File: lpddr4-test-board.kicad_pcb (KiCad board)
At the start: 8 copper layers, 117 x 81 mm, 261 parts, among them IC1 TPS54561, IC2 NCP380HMUAJAATBG, IC3 TPD8S009DSMR, J1 0878311420, J2 08B0-1X1T-36-F, J3 DC_SOCKET, J4 WE_629105150521, J5 61300611121, J6 685119134923, J7 1140084168, J8 61300411121, J9 ddr3-sodimm-slot-2-2013289-2, Q1 BC817W, Q2 BSS138AKA, Q3 BSS138AKA, Q4 BSS138AKA, Q5 BSS138AKA, Q6 BSS138AKA, U1 XC7K70T-FBG484, U10 REF3012AIDBZT, U12 FT2232HQ, U2 ASEM1-100.000MHZ-LC-T, U3 S25FL128SAGNFI000, U4 TPS65296, U5 TPS62823DLCT, U6 DP83848JSQ_NOPB, Y1 ABM8G-25.000MHZ-18-D2Y-T

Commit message: Activate B16
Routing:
- net Net-(J2-Pad8): track 0.00 -> 4.31 mm
- net GND: track 255.3 -> 257.7 mm, vias 218 -> 222
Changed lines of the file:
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@@
     (thickness 1.6)
     (drawings 130)
-    (tracks 4502)
+    (tracks 4514)
     (zones 0)
     (modules 261)
@@
   (via (at 103 128) (size 3.2) (drill 3) (layers F.Cu B.Cu) (net 0))
   (via (at 214 128) (size 3.2) (drill 3) (layers F.Cu B.Cu) (net 0))
+  (via (at 198.521 104.047) (size 0.5) (drill 0.2) (layers F.Cu B.Cu) (net 35))
+  (segment (start 198.511 103.455) (end 198.511 104.037) (width 0.15) (layer B.Cu) (net 35))
+  (via (at 200.426 104.047) (size 0.5) (drill 0.2) (layers F.Cu B.Cu) (net 35))
+  (segment (start 200.416 103.455) (end 200.416 104.037) (width 0.15) (layer B.Cu) (net 35))
+  (via (at 202.458 104.047) (size 0.5) (drill 0.2) (layers F.Cu B.Cu) (net 35))
+  (segment (start 202.448 103.455) (end 202.448 104.037) (width 0.15) (layer B.Cu) (net 35))
   (segment (start 173.536329 104.497157) (end 174.036329 104.997157) (width 0.15) (layer F.Cu) (net 392))
   (via blind (at 174.036329 104.997157) (size 0.5) (drill 0.2) (layers F.Cu GND1) (net 392) (status 40000))
@@
   (segment (start 171.536329 91.497157) (end 172.036329 90.997156) (width 0.15) (layer F.Cu) (net 19))
   (via (at 172.036329 90.997156) (size 0.5) (drill 0.2) (layers F.Cu B.Cu) (net 19) (status 40000))
+  (segment (start 207.465 101.47) (end 207.465 102.977) (width 0.15) (layer B.Cu) (net 21))
+  (segment (start 206.5736 103.8684) (end 206.5736 105.4102) (width 0.15) (layer B.Cu) (net 21))
+  (segment (start 207.465 102.977) (end 206.5736 103.8684) (width 0.15) (layer B.Cu) (net 21))
   (via (at 168.036329 90.997157) (size 0.5) (drill 0.2) (layers F.Cu B.Cu) (net 29) (status 40000))
   (segment (start 168.536329 91.497157) (end 168.036329 90.997157) (width 0.15) (layer F.Cu) (net 29))
@@
   (segment (start 207.528 70.273) (end 208.673 70.273) (width 0.15) (layer F.Cu) (net 35))
   (segment (start 208.673 70.273) (end 208.681 70.265) (width 0.15) (layer F.Cu) (net 35))
+  (via (at 204.49 104.047) (size 0.5) (drill 0.2) (layers F.Cu B.Cu) (net 35))
+  (segment (start 204.48 103.455) (end 204.48 104.037) (width 0.15) (layer B.Cu) (net 35))
+  (segment (start 204.48 104.037) (end 204.49 104.047) (width 0.15) (layer B.Cu) (net 35))
   (segment (start 163.536329 104.497157) (end 163.036329 104.997157) (width 0.15) (layer F.Cu) (net 36))
   (via (at 163.036329 104.997157) (size 0.5) (drill 0.2) (layers F.Cu B.Cu) (net 36) (status 40000))

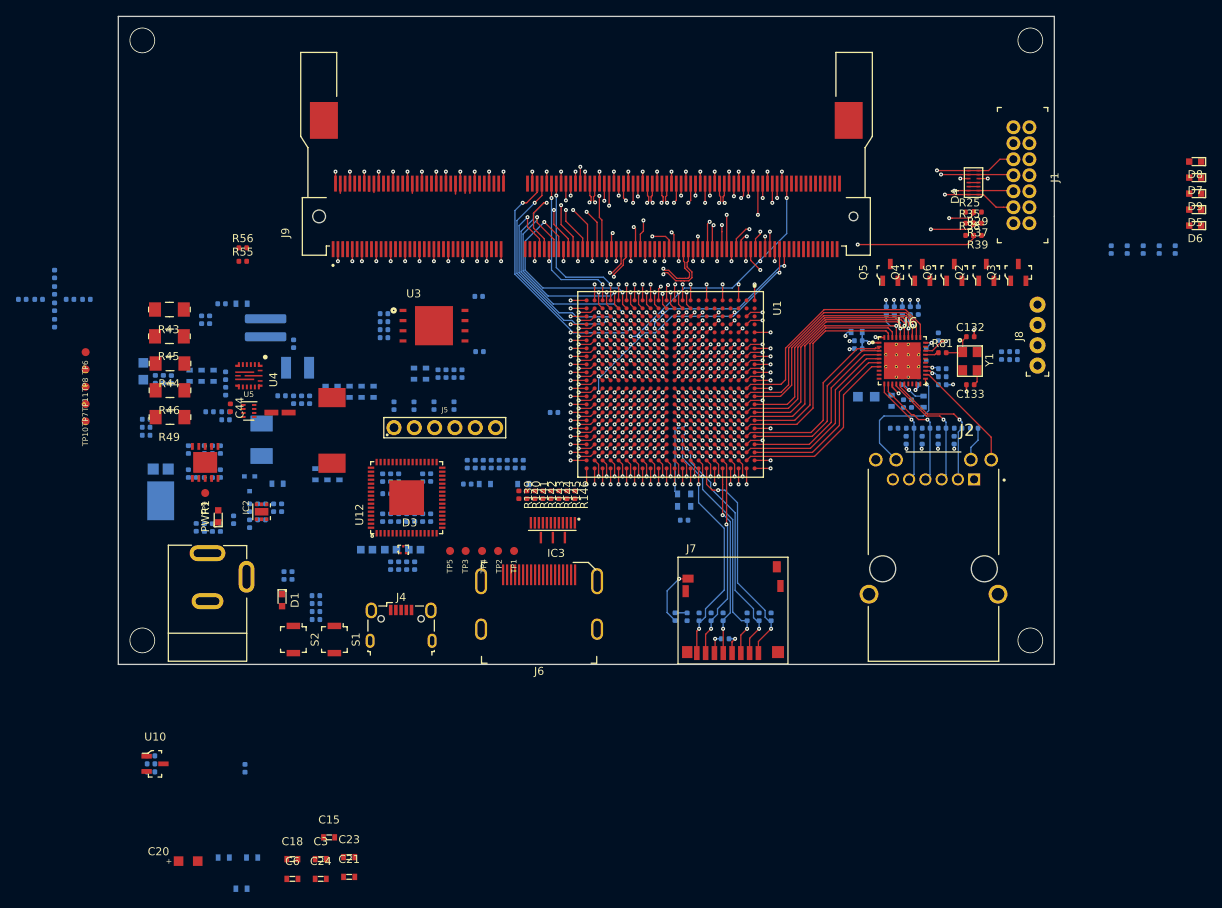
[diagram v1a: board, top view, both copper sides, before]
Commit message: Route SD card
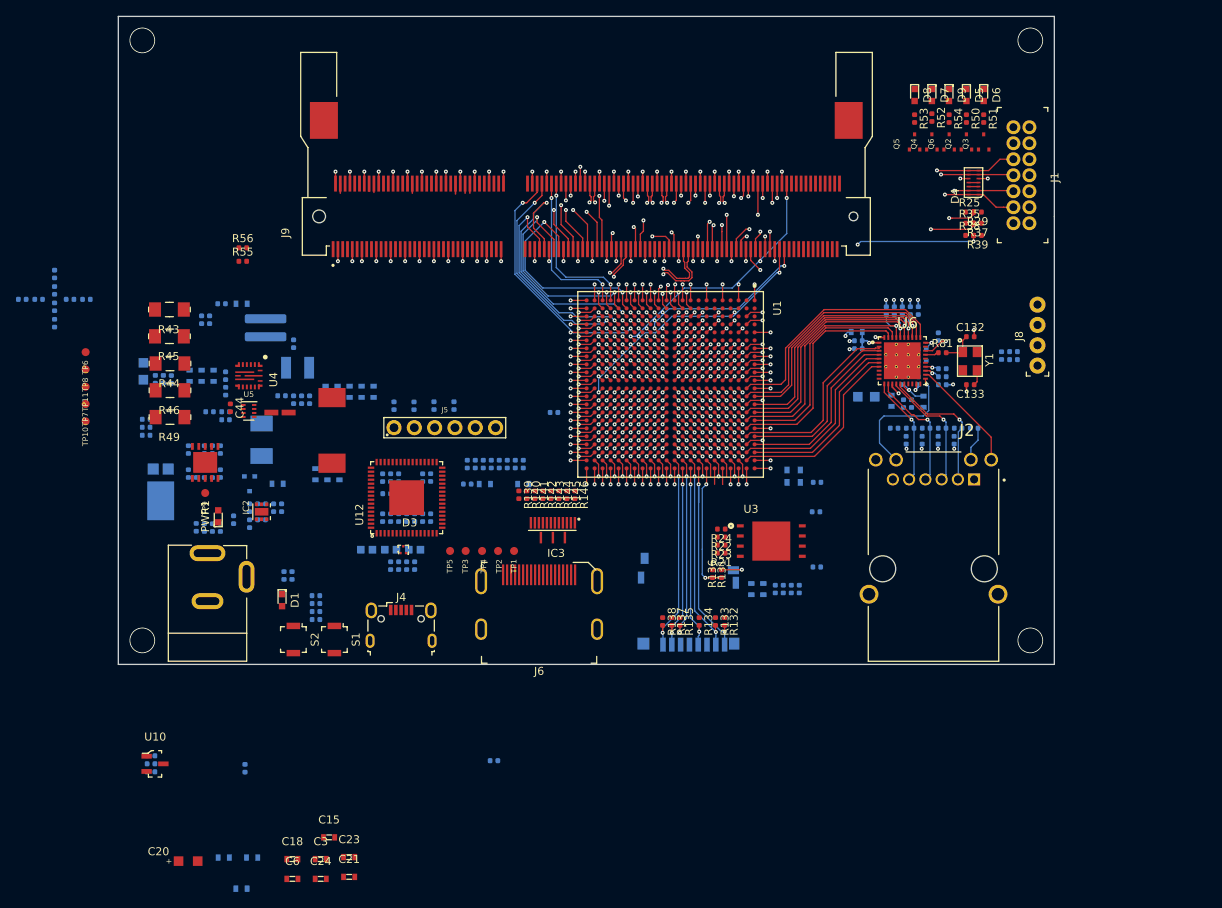
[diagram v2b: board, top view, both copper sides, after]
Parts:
- J7: moved to B.Cu
- Q2, Q3, Q4, Q5, Q6: value BSS138AKA -> BSS138APW; footprint lpddr4-test-board-footprints:SOT-23-3 -> antmicro-footprints:SC70-3
- R131, R132, R133, R134, R135, R136, R137, R138, R21, R22, R23, R24, R50, R51, R52, R53, R54: moved to F.Cu
- moved C5 50.0 mm to (187.2, 111.9)
- moved R10 50.0 mm to (183.1, 121.6)
- moved R20 50.0 mm to (182.1, 121.6)
- moved R21 50.0 mm to (175.4, 117.1)
- moved R22 50.0 mm to (175.4, 115.1)
- moved R23 50.0 mm to (175.4, 116.1)
- moved R24 50.0 mm to (175.4, 114.1)
- moved R26 50.0 mm to (179.1, 121.6)
- moved R27 50.0 mm to (180.6, 121.6)
- moved R33 50.0 mm to (185.1, 121.6)
- moved R34 50.0 mm to (184.1, 121.6)
- moved U3 50.0 mm to (181.6, 115.6)
- moved C10 50.0 mm to (187.3, 118.8)
- moved D8 36.1 mm to (199.5, 59.8), turned to 270 degrees
- moved D7 34.5 mm to (201.7, 59.8), turned to 270 degrees
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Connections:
- net DAT1 renamed SD_DAT1
- J7 pad 1: DAT2 -> SD_DAT2
- J7 pad 2: CD_DAT3 -> SD_DAT3
- J7 pad 3: MOSI_CMD -> SD_CMD
- J7 pad 5: SCK -> SD_CLK
- J7 pad 7: MISO_DAT0 -> SD_DAT0
- R131 pad 2: CD -> SD_CD
- R133 pad 2: MISO_DAT0 -> SD_DAT0
- R134 pad 2: SCK -> SD_CLK
- R135 pad 2: MOSI_CMD -> SD_CMD
- R136 pad 1: CD -> SD_CD
- R137 pad 2: CD_DAT3 -> SD_DAT3
- R138 pad 2: DAT2 -> SD_DAT2
- U1 pad A10: GND -> Net-(U1-PadA10)
- U1 pad A11: GND -> Net-(U1-PadA11)
- U1 pad A8: GND -> Net-(U1-PadA8)
- U1 pad A9: GND -> Net-(U1-PadA9)
- U1 pad B10: GND -> Net-(U1-PadB10)
- U1 pad B11: GND -> Net-(U1-PadB11)
- U1 pad B8: GND -> Net-(U1-PadB8)
- U1 pad C10: GND -> Net-(U1-PadC10)
- U1 pad C11: GND -> VCC3V3
- U1 pad C8: GND -> Net-(U1-PadC8)
- U1 pad C9: GND -> Net-(U1-PadC9)
- U1 pad D10: GND -> Net-(U1-PadD10)
- U1 pad D11: GND -> Net-(U1-PadD11)
- U1 pad D8: GND -> VCC3V3
- U1 pad D9: GND -> Net-(U1-PadD9)
- U1 pad E11: GND -> Net-(U1-PadE11)
- U1 pad E12: GND -> Net-(U1-PadE12)
- U1 pad E13: GND -> Net-(U1-PadE13)
- U1 pad E21: MISO_DAT0 -> Net-(U1-PadE21)
- U1 pad E22: SCK -> Net-(U1-PadE22)
- U1 pad E8: GND -> Net-(U1-PadE8)
- U1 pad E9: GND -> Net-(U1-PadE9)
- U1 pad F10: GND -> Net-(U1-PadF10)
- U1 pad F11: GND -> Net-(U1-PadF11)
- U1 pad F12: GND -> VCC3V3
- U1 pad F13: GND -> Net-(U1-PadF13)
- U1 pad F14: GND -> Net-(U1-PadF14)
- U1 pad F8: GND -> Net-(U1-PadF8)
- U1 pad F9: GND -> Net-(U1-PadF9)
- U1 pad G10: GND -> Net-(U1-PadG10)
- U1 pad G11: GND -> Net-(U1-PadG11)
- U1 pad G12: GND -> Net-(U1-PadG12)
- U1 pad G13: GND -> Net-(U1-PadG13)
- U1 pad G21: CD -> Net-(U1-PadG21)
- U1 pad G22: DAT2 -> SD_CD
- U1 pad G8: GND -> Net-(U1-PadG8)
- U1 pad G9: GND -> VCC3V3
- U1 pad H10: GND -> Net-(U1-PadH10)
- U1 pad H12: GND -> Net-(U1-PadH12)
- U1 pad H13: GND -> Net-(U1-PadH13)
- U1 pad H14: GND -> Net-(U1-PadH14)
- U1 pad H8: GND -> Net-(U1-PadH8)
- U1 pad H9: GND -> Net-(U1-PadH9)
- U1 pad J21: Net-(U1-PadJ21) -> SD_DAT0
- U1 pad J22: Net-(U1-PadJ22) -> SD_CLK
- U1 pad K17: MOSI_CMD -> Net-(U1-PadK17)
- U1 pad K19: CD_DAT3 -> Net-(U1-PadK19)
- U1 pad K21: Net-(U1-PadK21) -> SD_CMD
- U1 pad K22: Net-(U1-PadK22) -> SD_DAT3
- U1 pad L21: Net-(U1-PadL21) -> SD_DAT2
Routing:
- net GND: track 257.7 -> 217.8 mm, vias 222 -> 182
- net MOSI_CMD: track 32.6 -> 0.00 mm, vias 2 -> 0
- net CD_DAT3: track 30.8 -> 0.00 mm, vias 2 -> 0
- net DAT2: track 28.5 -> 0.00 mm, vias 2 -> 0
- net MISO_DAT0: track 25.6 -> 0.00 mm, vias 2 -> 0
- net SD_DAT0: track 0.00 -> 25.5 mm, vias 0 -> 2
- net SD_DAT2: track 0.00 -> 25.0 mm, vias 0 -> 2
- net SCK: track 24.1 -> 0.00 mm, vias 2 -> 0
- net SD_DAT3: track 0.00 -> 23.5 mm, vias 0 -> 2
- net SD_CLK: track 0.00 -> 23.3 mm, vias 0 -> 2
- net SD_CMD: track 0.00 -> 23.0 mm, vias 0 -> 2
- net SD_CD: track 0.00 -> 16.1 mm, vias 0 -> 2
- net GCLK100: track 10.5 -> 0.71 mm
- net QSPI_DQ2: track 0.71 -> 7.88 mm
- net QSPI_DQ3: track 0.71 -> 7.38 mm
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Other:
- board text removed: "Change to smaller footprint"
- board text removed: "Place between two power planes"

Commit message: Increase PCB height
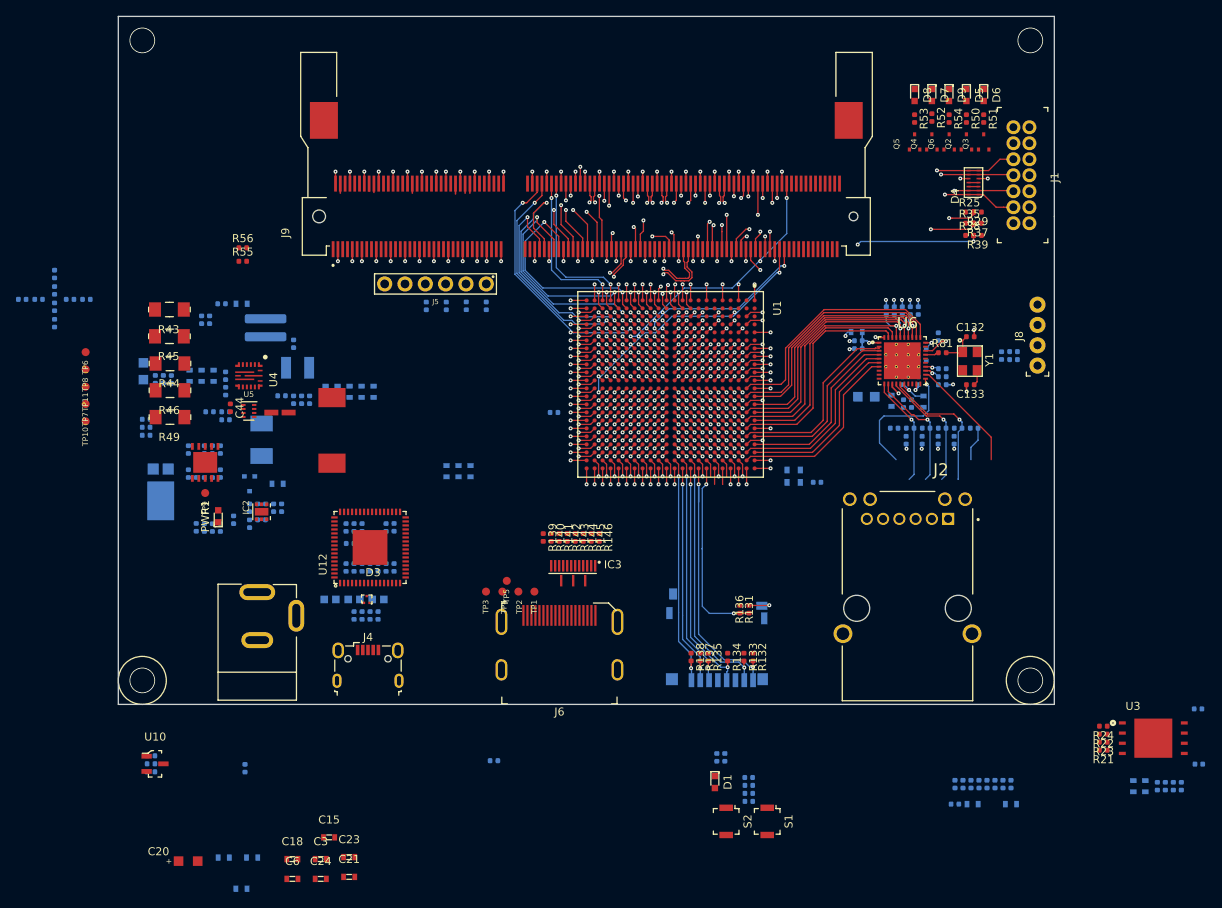
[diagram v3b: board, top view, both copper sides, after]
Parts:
- moved C1 72.9 mm to (204.6, 148.5)
- moved C2 72.9 mm to (206.8, 148.5)
- moved C4 72.9 mm to (211.6, 148.5)
- moved R1 72.9 mm to (204.6, 146.0)
- moved R2 72.9 mm to (205.6, 146.0)
- moved R3 72.9 mm to (206.6, 146.0)
- moved R4 72.9 mm to (207.6, 146.0)
- moved R5 72.9 mm to (208.6, 146.0)
- moved R6 72.9 mm to (209.6, 146.0)
- moved R7 72.9 mm to (210.6, 146.0)
- moved R8 72.9 mm to (211.6, 146.0)
- moved R15 58.7 mm to (178.8, 146.1)
- moved R17 58.7 mm to (178.8, 147.1)
- moved R30 58.7 mm to (178.8, 148.1)
- moved R31 58.7 mm to (174.8, 142.6)
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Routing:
- net SD_CD: track 16.1 -> 24.0 mm
- net SD_DAT0: track 25.5 -> 32.7 mm
- net SD_DAT1: track 26.7 -> 33.9 mm
- net SD_CMD: track 23.0 -> 29.8 mm
- net SD_CLK: track 23.3 -> 29.8 mm
- net SD_DAT3: track 23.5 -> 29.1 mm
- net SD_DAT2: track 25.0 -> 29.8 mm
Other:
- board size 117 x 81 mm -> 117 x 86 mm

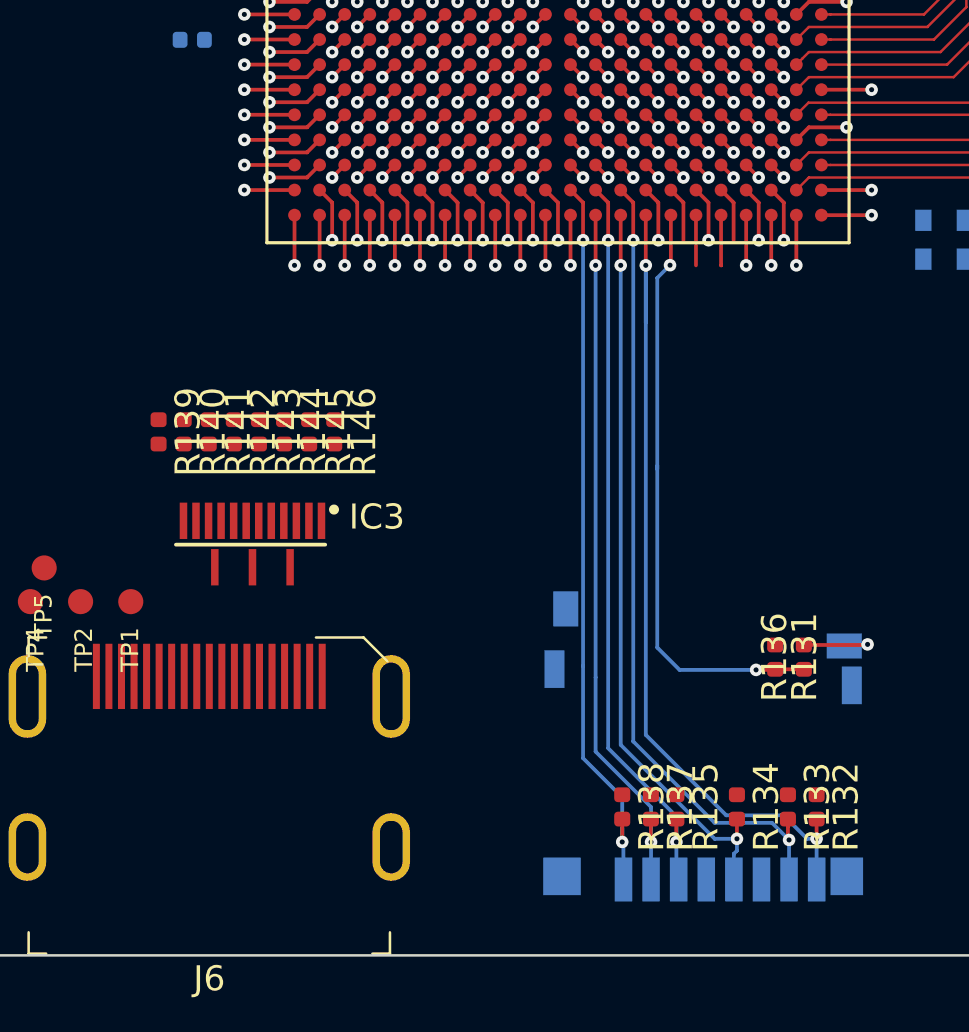
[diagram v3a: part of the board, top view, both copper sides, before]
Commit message: Move SD to B15
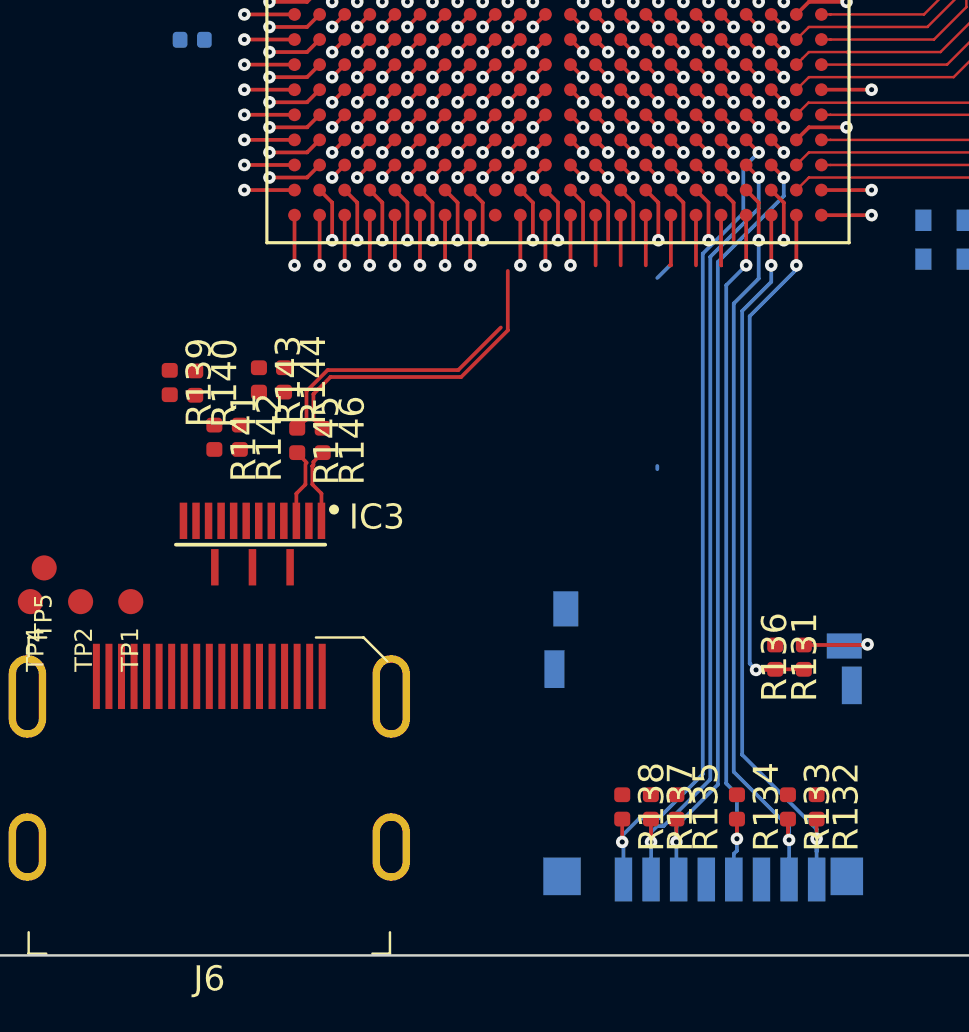
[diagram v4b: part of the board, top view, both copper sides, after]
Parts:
- moved R143 2.07 mm to (157.1, 113.1)
- moved R144 2.07 mm to (158.1, 113.1)
- moved R139 2.02 mm to (153.6, 113.2)
- moved R140 2.00 mm to (154.6, 113.2)
- moved R145 0.59 mm to (158.6, 115.5)
- moved R146 0.57 mm to (159.7, 115.5)
- moved R142 0.32 mm to (156.4, 115.3)
- moved R141 0.31 mm to (155.3, 115.3)
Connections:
- U1 pad B22: Net-(U1-PadB22) -> SD_CD
- U1 pad C20: Net-(U1-PadC20) -> SD_CMD
- U1 pad C22: Net-(U1-PadC22) -> SD_DAT1
- U1 pad D19: Net-(U1-PadD19) -> SD_DAT2
- U1 pad D20: Net-(U1-PadD20) -> SD_DAT3
- U1 pad D21: Net-(U1-PadD21) -> SD_DAT0
- U1 pad D22: Net-(U1-PadD22) -> SD_CLK
- U1 pad G22: SD_CD -> Net-(U1-PadG22)
- U1 pad H22: SD_DAT1 -> Net-(U1-PadH22)
- U1 pad J21: SD_DAT0 -> Net-(U1-PadJ21)
- U1 pad J22: SD_CLK -> Net-(U1-PadJ22)
- U1 pad K21: SD_CMD -> Net-(U1-PadK21)
- U1 pad K22: SD_DAT3 -> Net-(U1-PadK22)
- U1 pad L21: SD_DAT2 -> Net-(U1-PadL21)
- U1 pad N17: TMDS_D2_N -> Net-(U1-PadN17)
- U1 pad P16: TMDS_D2_P -> Net-(U1-PadP16)
- U1 pad P17: TMDS_D0_N -> Net-(U1-PadP17)
- U1 pad P21: TMDS_D1_P -> TMDS_D2_P
- U1 pad P22: TMDS_D1_N -> TMDS_D2_N
- U1 pad R17: TMDS_D0_P -> Net-(U1-PadR17)
- U1 pad R21: TMDS_CLK_P -> TMDS_D1_P
- U1 pad R22: TMDS_CLK_N -> TMDS_D1_N
- U1 pad T19: USR_LED1 -> Net-(U1-PadT19)
- U1 pad T21: USR_LED2 -> Net-(U1-PadT21)
- U1 pad U21: USR_LED3 -> TMDS_D0_N
- U1 pad U22: USR_LED4 -> TMDS_D0_P
- U1 pad V22: USR_LED5 -> Net-(U1-PadV22)
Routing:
- net TMDS_D2_P: track 0.71 -> 12.7 mm, vias 1 -> 0
- net TMDS_D2_N: track 0.71 -> 10.4 mm, vias 1 -> 0
- net SD_DAT1: track 33.9 -> 29.5 mm
- net SD_DAT2: track 29.8 -> 33.3 mm
- net C_TMDS_D2_P: track 0.00 -> 3.07 mm
- net C_TMDS_D2_N: track 0.00 -> 2.97 mm
- net SD_DAT0: track 32.7 -> 30.2 mm
- net SD_DAT3: track 29.1 -> 31.5 mm
- net USR_LED2: track 2.21 -> 0.00 mm, vias 1 -> 0
- net Net-(U1-PadT21): track 0.00 -> 2.21 mm, vias 0 -> 1
- net Net-(U1-PadD21): track 2.21 -> 0.00 mm, vias 1 -> 0
- net TMDS_CLK_P: track 2.21 -> 0.00 mm, vias 1 -> 0
- net Net-(U1-PadL21): track 0.00 -> 2.21 mm
- net Net-(U1-PadK21): track 0.00 -> 2.21 mm
- net Net-(U1-PadJ21): track 0.00 -> 2.21 mm
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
